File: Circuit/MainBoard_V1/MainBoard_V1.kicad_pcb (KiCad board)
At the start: 2 copper layers, 56 x 65 mm, 91 parts, among them J1 Conn_01x07, J10 Conn_01x04, J11 Conn_01x04, J12 Conn_01x04, J2 Raspberry_Pi_2_3, J3 Conn_01x04, J4 Conn_01x04, J5 Conn_01x04, J6 Conn_01x04, J7 Conn_01x04, J8 Conn_01x04, J9 Conn_01x04, Q1 Q_PMOS_GDS, Q2 Q_PMOS_GDS, Q3 BSS138, SW1 SW_Push, SW2 SW_Push, SW5 SW_Push, SW6 SW_Push, U1 LM1117MP-3.3, U11 LM78M05_TO252, U2 STM32F446RETx, U3 MPU-6050, Y1 CSTNE16M0V530000R0

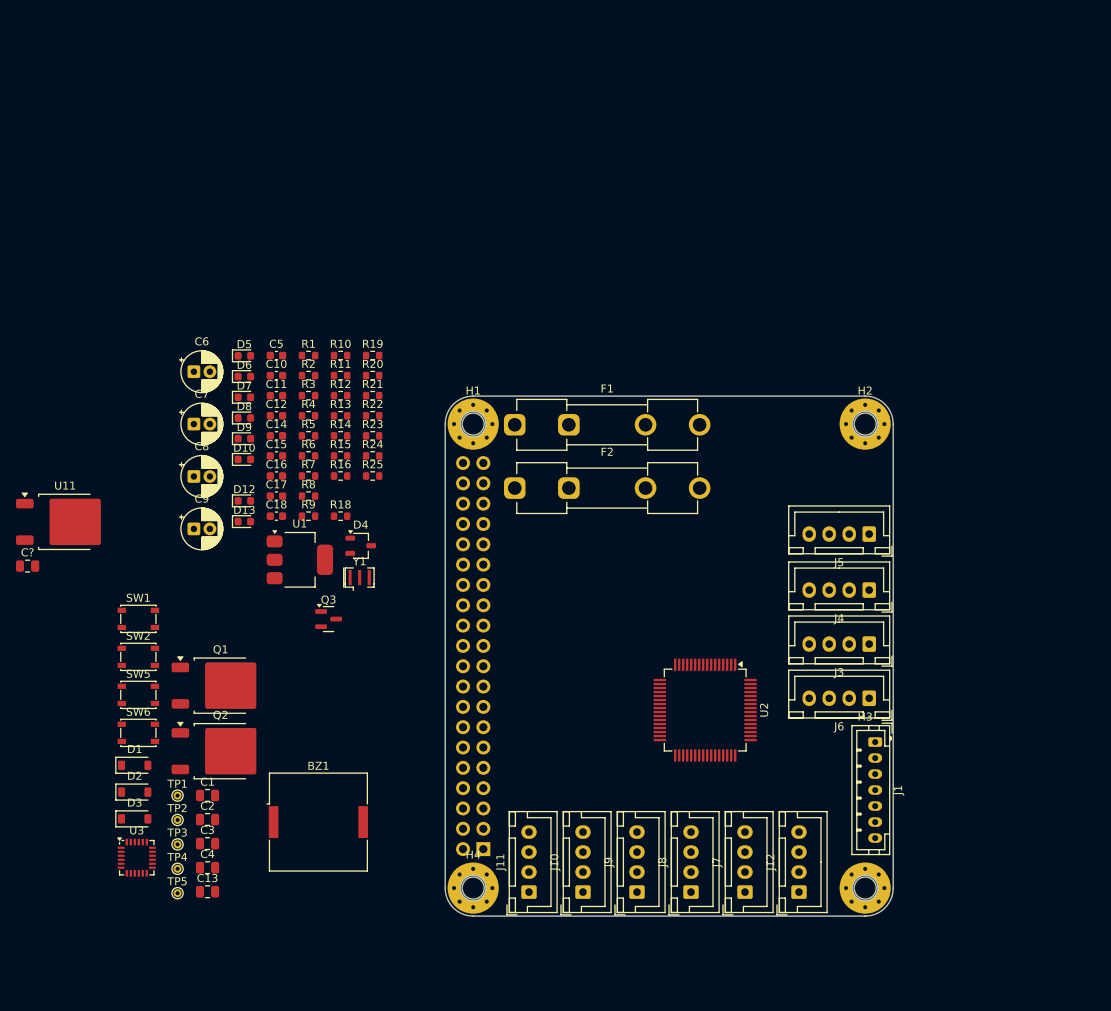
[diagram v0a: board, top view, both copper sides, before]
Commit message: 配線と配置を進めた
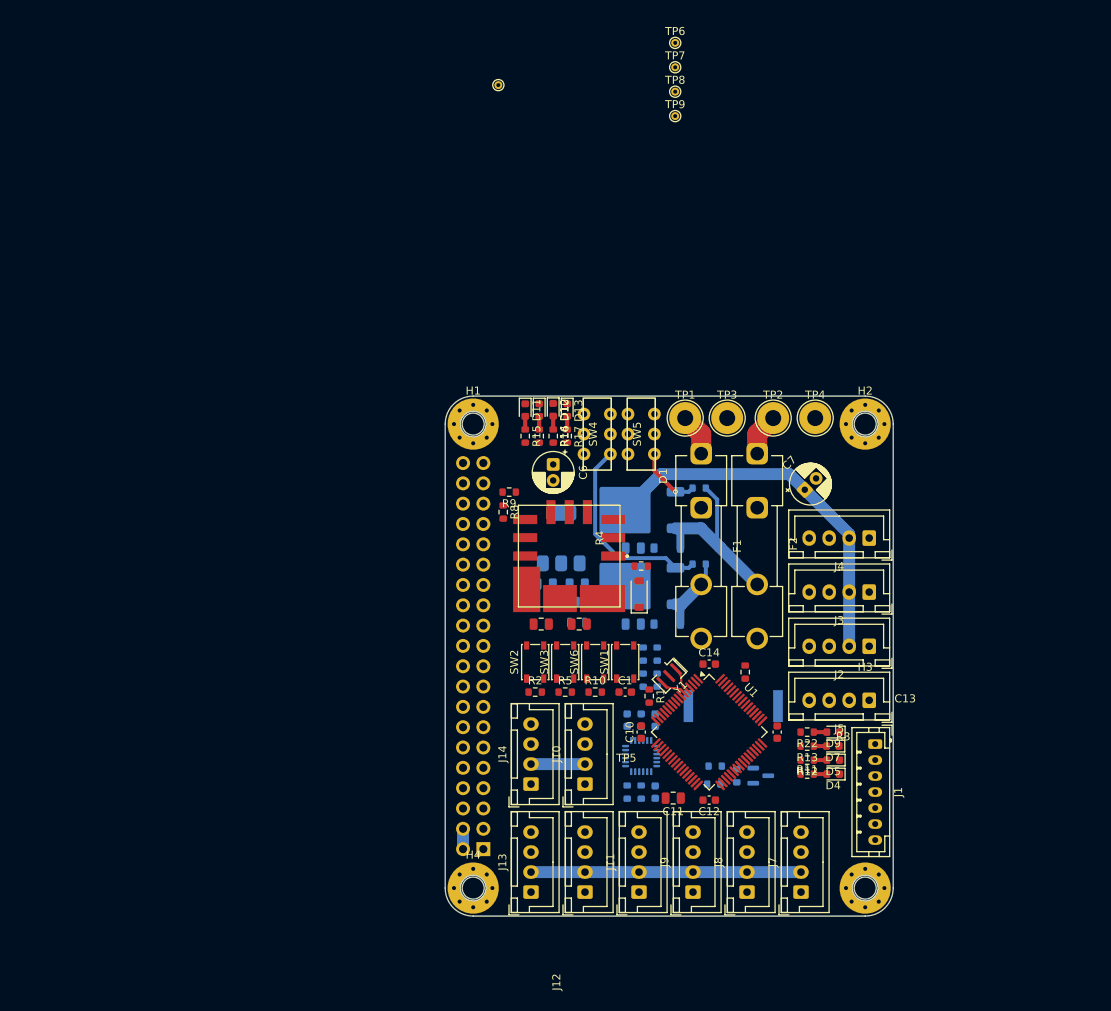
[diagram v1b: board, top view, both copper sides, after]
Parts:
- removed C?: 10u, Capacitor_SMD:C_0805_2012Metric
- removed U11: LM78M05_TO252, Package_TO_SOT_SMD:TO-252-2
- added D11: LED, LED_SMD:LED_0603_1608Metric, F.Cu at (109.5, 122.2)
- added J13: Conn_01x04, Connector_JST:JST_XH_B4B-XH-A_1x04_P2.50mm_Vertical, F.Cu at (110.2, 182.5)
- added J14: Conn_01x04, Connector_JST:JST_XH_B4B-XH-A_1x04_P2.50mm_Vertical, F.Cu at (110.2, 169.0)
- added MD1: OKL-T_6-W12N-C, 0-MyLibrary:MURATA_OKL-T-6-W12N-C_0, F.Cu at (115.0, 140.5)
- added R17: 10k, Resistor_SMD:R_0603_1608Metric, F.Cu at (114.8, 125.5)
- added R26: 4.7k, Resistor_SMD:R_0603_1608Metric, B.Cu at (122.2, 170.0)
- added R27: 4.7k, Resistor_SMD:R_0603_1608Metric, B.Cu at (124.0, 170.0)
- added SW3: SW_Push, Button_Switch_SMD:SW_SPST_PTS810, F.Cu at (114.5, 153.8)
- added SW4: SW_Slide_DPDT, 0-MyLibrary:IS-2235, F.Cu at (118.5, 125.2)
- added TP6: TestPoint, TestPoint:TestPoint_THTPad_D1.0mm_Drill0.5mm, F.Cu at (128.2, 76.3)
- added TP7: TestPoint, TestPoint:TestPoint_THTPad_D1.0mm_Drill0.5mm, F.Cu at (128.2, 79.4)
- added TP8: TestPoint, TestPoint:TestPoint_THTPad_D1.0mm_Drill0.5mm, F.Cu at (128.2, 82.5)
- added TP9: TestPoint, TestPoint:TestPoint_THTPad_D1.0mm_Drill0.5mm, F.Cu at (128.2, 85.5)
- BZ1, C15, C16, C17, C18, C4, D2, D3, Q1, Q2, Q3, R19, R21, R6, R7, U3: moved to B.Cu
- C1: value 10u -> 0.1uf; footprint Capacitor_SMD:C_0805_2012Metric -> Capacitor_SMD:C_0603_1608Metric
- C11: value 0.1uf -> 4.7u; footprint Capacitor_SMD:C_0603_1608Metric -> Capacitor_SMD:C_0805_2012Metric
- C13: value 4.7u -> 0.1uf; footprint Capacitor_SMD:C_0805_2012Metric -> Capacitor_SMD:C_0603_1608Metric
- C5: value 0.1uf -> 10u; footprint Capacitor_SMD:C_0603_1608Metric -> Capacitor_SMD:C_0805_2012Metric; moved to B.Cu
- C8, C9: value 100uf -> 10u; footprint Capacitor_THT:CP_Radial_D5.0mm_P2.00mm -> Capacitor_SMD:C_0805_2012Metric; moved to B.Cu
- D4: value CH213K -> LED; footprint Package_TO_SOT_SMD:TSOT-23 -> LED_SMD:LED_0603_1608Metric
- D6: value LED -> 1N4148W; footprint LED_SMD:LED_0603_1608Metric -> Diode_SMD:D_SOD-123; moved to B.Cu
- D8: value LED -> CH213K; footprint LED_SMD:LED_0603_1608Metric -> Package_TO_SOT_SMD:TSOT-23; moved to B.Cu
- J2: value Raspberry_Pi_2_3 -> Conn_01x04; footprint 0-MyLibrary:raspberreyPi_2_3 -> Connector_JST:JST_XH_B4B-XH-A_1x04_P2.50mm_Vertical
- J6: value Conn_01x04 -> Raspberry_Pi_2_3; footprint Connector_JST:JST_XH_B4B-XH-A_1x04_P2.50mm_Vertical -> 0-MyLibrary:raspberreyPi_2_3
- R12, R8: value 10k -> 1k
- R16: value 1k -> 10k
- R18, R20: value 1k -> 10k; moved to B.Cu
- R22: value 10 -> 1k
- R23: value 10k -> 1k; moved to B.Cu
- R24: value 4.7k -> 10; moved to B.Cu
- R25: value 4.7k -> 10k; moved to B.Cu
- R9: value 10k -> 330
- SW5: value SW_Push -> SW_Slide_DPDT; footprint Button_Switch_SMD:SW_SPST_PTS810 -> 0-MyLibrary:IS-2235
- TP1, TP2, TP3, TP4: footprint TestPoint:TestPoint_THTPad_D1.0mm_Drill0.5mm -> TestPoint:TestPoint_THTPad_D4.0mm_Drill2.0mm
- U1: value LM1117MP-3.3 -> STM32F446RETx; footprint Package_TO_SOT_SMD:SOT-223-3_TabPin2 -> Package_QFP:LQFP-64_10x10mm_P0.5mm
- U2: value STM32F446RETx -> LM1117MP-3.3; footprint Package_QFP:LQFP-64_10x10mm_P0.5mm -> Package_TO_SOT_SMD:SOT-223-3_TabPin2; moved to B.Cu
- moved TP5 108.7 mm to (106.1, 81.6)
- moved TP4 97.6 mm to (145.8, 123.2)
- moved TP2 89.8 mm to (140.5, 123.2)
- moved D5 89.3 mm to (148.0, 166.0), turned to 180 degrees
- moved TP3 86.9 mm to (134.8, 123.2)
- moved D7 85.5 mm to (148.0, 164.2), turned to 180 degrees
- moved D9 82.2 mm to (148.0, 162.5), turned to 180 degrees
- moved TP1 79.1 mm to (129.5, 123.2)
- moved C7 76.8 mm to (144.4, 132.2), turned to 45 degrees
- moved R11 76.7 mm to (144.8, 167.8), turned to 180 degrees
- moved D3 74.7 mm to (127.2, 139.5), turned to 180 degrees
- moved R12 74.0 mm to (144.8, 166.0), turned to 180 degrees
- moved C13 73.9 mm to (141.0, 162.5), turned to -90 degrees
- moved C12 72.3 mm to (132.5, 171.0), turned to 180 degrees
- moved R13 71.5 mm to (144.8, 164.2), turned to 180 degrees
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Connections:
- C1 pad 1: VCC -> GND
- C1 pad 2: GND -> NRST
- C11 pad 1: +3V3 -> Net-(U1-VCAP_1)
- C11 pad 2: GND1 -> GND
- C12 pad 1: GND1 -> GND
- C13 pad 1: Net-(U2-VCAP_1) -> GND
- C13 pad 2: GND -> +3V3
- C15 pad 1: GND -> +3V3
- C15 pad 2: +3V3 -> GND
- C2 pad 1: VCCP -> GND
- C2 pad 2: GNDP -> VCC
- C3 pad 2: +5V -> GND
- C4 pad 1: Net-(D1-A) -> VCC
- C5 pad 1: GND -> VCCP
- C5 pad 2: NRST -> GNDP
- C8 pad 1: VCC -> GND
- C8 pad 2: GND -> +5V
- C9 pad 1: VCCP -> Net-(D6-A)
- C9 pad 2: GNDP -> GND
- D1 pad 1: +5V -> VCC
- D13 pad 1: GND -> GNDP
- D4 pad 2: +3V3 -> Net-(D4-A)
- D6 pad 1: GNDP -> +5V
- D8 pad 2: Net-(D8-A) -> +3V3
- J10 pad 3: TRIG4 -> TRIG7
- J10 pad 4: ECHO4 -> ECHO7
- J11 pad 3: TRIG5 -> TRIG4
- J11 pad 4: ECHO5 -> ECHO4
- J12 pad 3: TRIG6 -> TRIG5
- J12 pad 4: ECHO6 -> ECHO5
- J2 pad 1: Net-(J2-3V3-Pad1) -> GND
- J2 pad 2: +5V -> VCCP
- J2 pad 3: unconnected-(J2-SDA/GPIO2-Pad3) -> TX2
- J2 pad 4: +5V -> RX2
- J3 pad 3: TX2 -> TX3
- J3 pad 4: RX2 -> RX3
- J4 pad 3: TX3 -> TX4
- J4 pad 4: RX3 -> RX4
- J5 pad 2: VCCP -> +3V3
- J5 pad 3: TX4 -> TX5
- J5 pad 4: RX4 -> RX5
- J6 pad 1: GND -> Net-(J6-3V3-Pad1)
- J6 pad 2: +3V3 -> +5V
- J6 pad 3: TX5 -> unconnected-(J6-SDA/GPIO2-Pad3)
- J6 pad 4: RX5 -> +5V
- R1 pad 1: Net-(D2-K) -> NRST
- R1 pad 2: Net-(Q1-G) -> +3V3
- R10 pad 1: VOLTAGE1 -> BTN3
- R10 pad 2: VCC -> GND
- R11 pad 1: GND -> Net-(D4-A)
- R11 pad 2: VOLTAGE1 -> STM_LED1
- R12 pad 1: VOLTAGE1 -> Net-(D5-A)
- R12 pad 2: VCCP -> STM_LED2
- R13 pad 1: GND2 -> Net-(D7-A)
- R13 pad 2: VOLTAGE1 -> STM_LED3
- R14 pad 1: Net-(D7-A) -> Net-(D10-A)
- R14 pad 2: STM_LED1 -> +3V3
- R15 pad 1: Net-(D9-A) -> Net-(D11-A)
- R15 pad 2: +3V3 -> +5V
- R16 pad 1: Net-(D10-A) -> Net-(D12-A)
- R16 pad 2: +5V -> VCC
- R18 pad 1: Net-(D8-A) -> VOLTAGE
- R18 pad 2: STM_LED2 -> VCC
- R19 pad 1: Net-(D12-A) -> GND
- R19 pad 2: STM_LED3 -> VOLTAGE
- R2 pad 1: Net-(D3-K) -> BTN1
- R2 pad 2: Net-(Q2-G) -> GND
- R20 pad 1: Net-(D13-A) -> VOLTAGEP
- R20 pad 2: STM_LED4 -> VCCP
- R21 pad 1: Net-(BZ1--) -> GND2
- R21 pad 2: VCC -> VOLTAGEP
- R22 pad 1: BUZZER -> Net-(D9-A)
- R22 pad 2: Net-(Q3-G) -> STM_LED4
- R23 pad 1: GND -> Net-(BZ1--)
- R23 pad 2: Net-(Q3-G) -> VCC
- R24 pad 1: +3V3 -> BUZZER
- R24 pad 2: SDA -> Net-(Q3-G)
- R25 pad 1: +3V3 -> GND
- R25 pad 2: SCL -> Net-(Q3-G)
- R3 pad 1: NRST -> GND
- R3 pad 2: +3V3 -> Net-(U1-BOOT0)
- R4 pad 1: BTN1 -> VCC
- R4 pad 2: GND -> Net-(MD1-~{ON}/OFF_CONTROL)
- R5 pad 1: GND -> BTN2
- R5 pad 2: Net-(U2-BOOT0) -> GND
- R6 pad 1: BTN2 -> Net-(D2-K)
- R6 pad 2: GND -> Net-(Q1-G)
- R7 pad 1: BTN3 -> Net-(D3-K)
- R7 pad 2: GND -> Net-(Q2-G)
- R8 pad 1: Net-(D5-A) -> Net-(R8-Pad1)
- R8 pad 2: VCC -> Net-(MD1-TRIM)
- R9 pad 1: Net-(D6-A) -> GND
- R9 pad 2: VCCP -> Net-(R8-Pad1)
- SW5 pad 1: BTN2 -> Net-(Q2-G)
- SW5 pad 2: +3V3 -> GNDP
- TP1 pad 1: SDA -> +BATT
- TP2 pad 1: SCL -> +BATTP
- TP3 pad 1: +5V -> GND
- TP4 pad 1: +3V3 -> GNDP
- TP5 pad 1: GND -> SDA
- U1 pad 1: GND -> +3V3
- U1 pad 2: Net-(D1-A) -> unconnected-(U1-PC13-Pad2)
- U1 pad 3: +5V -> unconnected-(U1-PC14-Pad3)
- U2 pad 1: +3V3 -> GND
- U2 pad 2: unconnected-(U2-PC13-Pad2) -> Net-(D6-A)
- U2 pad 3: unconnected-(U2-PC14-Pad3) -> +5V
- Y1 pad 1: Net-(U2-PH0) -> Net-(U1-PH0)
- Y1 pad 3: Net-(U2-PH1) -> Net-(U1-PH1)
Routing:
- net VCCP: track 0.00 -> 47.0 mm
- net +3V3: track 0.00 -> 40.5 mm
- net Net-(Q1-G): track 0.00 -> 24.9 mm
- net Net-(D3-K): track 0.00 -> 23.5 mm
- net Net-(D2-K): track 0.00 -> 9.75 mm
- net Net-(Q2-G): track 0.00 -> 8.14 mm, vias 0 -> 1
- net +BATTP: track 0.00 -> 5.27 mm
- net +BATT: track 0.00 -> 5.27 mm
- net Net-(U1-PH1): track 0.00 -> 3.12 mm
- net Net-(U1-PH0): track 0.00 -> 3.05 mm
- net +5V: track 0.00 -> 2.54 mm
- net Net-(D12-A): track 0.00 -> 1.67 mm
- net Net-(D9-A): track 0.00 -> 1.64 mm
- net Net-(D5-A): track 0.00 -> 1.64 mm
- net Net-(D4-A): track 0.00 -> 1.64 mm
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
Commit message: LED用のコネクタ追加
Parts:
- added J15: Conn_01x02, Connector_JST:JST_XH_B2B-XH-A_1x02_P2.50mm_Vertical, F.Cu at (117.0, 160.5)
- added J16: Conn_01x02, Connector_JST:JST_XH_B2B-XH-A_1x02_P2.50mm_Vertical, F.Cu at (110.2, 160.5)
- added Q4: BSS138, Package_TO_SOT_SMD:SOT-23, B.Cu at (114.0, 168.0)
- added Q5: BSS138, Package_TO_SOT_SMD:SOT-23, B.Cu at (107.2, 168.0)
- added Q6: BSS138, Package_TO_SOT_SMD:SOT-23, B.Cu at (114.0, 159.5)
- added Q7: BSS138, Package_TO_SOT_SMD:SOT-23, B.Cu at (107.2, 159.5)
- added R28: 10, Resistor_SMD:R_0603_1608Metric, B.Cu at (107.2, 163.5)
- added R29: 10k, Resistor_SMD:R_0603_1608Metric, B.Cu at (107.2, 165.2)
- added R30: 10, Resistor_SMD:R_0603_1608Metric, B.Cu at (114.0, 155.0)
- added R31: 10k, Resistor_SMD:R_0603_1608Metric, B.Cu at (114.0, 156.8)
- added R32: 4.7k, Resistor_SMD:R_0603_1608Metric, B.Cu at (123.2, 170.0)
- added R33: 4.7k, Resistor_SMD:R_0603_1608Metric, B.Cu at (125.0, 170.0)
- added R34: 10, Resistor_SMD:R_0603_1608Metric, B.Cu at (107.2, 155.0)
- added R35: 10k, Resistor_SMD:R_0603_1608Metric, B.Cu at (107.2, 156.8)
- J13, J14: value Conn_01x04 -> Conn_01x02; footprint Connector_JST:JST_XH_B4B-XH-A_1x04_P2.50mm_Vertical -> Connector_JST:JST_XH_B2B-XH-A_1x02_P2.50mm_Vertical
- R26: value 4.7k -> 10
- R27: value 4.7k -> 10k
- moved TP5 23.5 mm to (128.2, 73.8)
- moved C6 21.0 mm to (108.2, 149.5)
- moved J10 15.1 mm to (123.7, 182.5)
- moved J13 15.1 mm to (117.0, 169.0)
- moved R27 11.1 mm to (114.0, 165.2), turned to 180 degrees
- moved R26 10.5 mm to (114.0, 163.5), turned to 180 degrees
- moved J11 6.75 mm to (117.0, 182.5)
- moved J12 6.75 mm to (110.2, 182.5)
- moved C1 3.95 mm to (124.2, 154.2)
- moved R10 3.95 mm to (120.5, 154.2)
- moved R2 3.95 mm to (113.0, 154.2)
- moved R5 3.95 mm to (116.8, 154.2)
- moved SW1 3.95 mm to (124.2, 150.5)
- moved SW2 3.95 mm to (113.0, 150.5)
- moved SW3 3.95 mm to (116.8, 150.5)
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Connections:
- J10 pad 3: TRIG7 -> TRIG4
- J10 pad 4: ECHO7 -> ECHO4
- J11 pad 3: TRIG4 -> TRIG5
- J11 pad 4: ECHO4 -> ECHO5
- J12 pad 3: TRIG5 -> TRIG6
- J12 pad 4: ECHO5 -> ECHO6
- J13 pad 1: GND -> LED1
- J13 pad 2: +3V3 -> +5V
- J14 pad 1: GND -> LED2
- J14 pad 2: +3V3 -> +5V
- R26 pad 1: +3V3 -> LED1_SIG
- R26 pad 2: SDA -> Net-(Q4-G)
- R27 pad 1: +3V3 -> GND
- R27 pad 2: SCL -> Net-(Q4-G)
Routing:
- net +3V3: track 40.5 -> 0.00 mm

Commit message: 配線進捗
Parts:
- moved R10 58.5 mm to (179.0, 154.0)
- moved R5 58.5 mm to (175.2, 154.0)
- moved SW3 58.5 mm to (175.2, 150.2)
- moved SW6 58.5 mm to (179.0, 150.2)
- moved C1 30.9 mm to (109.2, 127.2)
- moved SW1 30.9 mm to (109.2, 123.5)
- moved R2 27.0 mm to (113.2, 127.2)
- moved SW2 27.0 mm to (113.2, 123.5)
- moved C6 17.9 mm to (90.5, 147.3)
- moved C13 14.8 mm to (127.0, 157.8), turned to -135 degrees
- moved J4 13.5 mm to (152.5, 151.8)
- moved J2 13.5 mm to (152.5, 138.3)
- moved D10 9.30 mm to (112.2, 131.5)
- moved D11 9.30 mm to (110.5, 131.5)
- moved D12 9.30 mm to (114.0, 131.5)
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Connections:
- J10 pad 3: TRIG4 -> ECHO4
- J10 pad 4: ECHO4 -> TRIG4
- J11 pad 3: TRIG5 -> ECHO5
- J11 pad 4: ECHO5 -> TRIG5
- J12 pad 3: TRIG6 -> ECHO6
- J12 pad 4: ECHO6 -> TRIG6
- J3 pad 3: TX3 -> TX4
- J3 pad 4: RX3 -> RX4
- J4 pad 3: TX4 -> TX5
- J4 pad 4: RX4 -> RX5
- J5 pad 3: TX5 -> TX3
- J5 pad 4: RX5 -> RX3
- J7 pad 3: TRIG1 -> ECHO1
- J7 pad 4: ECHO1 -> TRIG1
- J8 pad 3: TRIG2 -> ECHO2
- J8 pad 4: ECHO2 -> TRIG2
- J9 pad 3: TRIG3 -> ECHO3
- J9 pad 4: ECHO3 -> TRIG3
- U1 pad 22: unconnected-(U1-PA6-Pad22) -> LED4_SIG
- U1 pad 23: unconnected-(U1-PA7-Pad23) -> LED3_SIG
- U1 pad 26: unconnected-(U1-PB0-Pad26) -> LED2_SIG
- U1 pad 27: unconnected-(U1-PB1-Pad27) -> LED1_SIG
- U1 pad 28: unconnected-(U1-PB2-Pad28) -> TRIG6
- U1 pad 29: unconnected-(U1-PB10-Pad29) -> ECHO6
- U1 pad 33: unconnected-(U1-PB12-Pad33) -> TRIG5
- U1 pad 34: unconnected-(U1-PB13-Pad34) -> ECHO5
- U1 pad 35: unconnected-(U1-PB14-Pad35) -> TRIG4
- U1 pad 36: unconnected-(U1-PB15-Pad36) -> ECHO4
- U1 pad 37: TX6 -> RAS_RX
- U1 pad 38: RX6 -> RAS_TX  
- U1 pad 39: unconnected-(U1-PC8-Pad39) -> TRIG3
- U1 pad 40: unconnected-(U1-PC9-Pad40) -> ECHO3
- U1 pad 41: unconnected-(U1-PA8-Pad41) -> ECHO2
- U1 pad 42: TX1 -> PC_RX
- U1 pad 43: RX1 -> PC_TX
- U1 pad 44: unconnected-(U1-PA11-Pad44) -> TRIG2
- U1 pad 45: unconnected-(U1-PA12-Pad45) -> ECHO1
- U1 pad 50: unconnected-(U1-PA15-Pad50) -> TRIG1
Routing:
- net RAS_TX  : track 0.00 -> 34.2 mm, vias 0 -> 1
- net RAS_RX: track 0.00 -> 33.7 mm, vias 0 -> 1
- net RX2: track 0.00 -> 32.1 mm
- net TX2: track 0.00 -> 31.0 mm
- net TX4: track 0.00 -> 25.0 mm
- net RX4: track 0.00 -> 24.2 mm
- net SWDIO: track 0.00 -> 24.0 mm
- net PC_RX: track 0.00 -> 23.6 mm, vias 0 -> 1
- net PC_TX: track 0.00 -> 22.0 mm, vias 0 -> 1
- net ECHO6: track 0.00 -> 21.9 mm
- net VCC: track 0.00 -> 21.8 mm
- net TRIG6: track 0.00 -> 21.0 mm
- net +5V: track 2.54 -> 21.8 mm
- net TX5: track 0.00 -> 18.2 mm
- net ECHO5: track 0.00 -> 16.7 mm
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
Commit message: 進捗
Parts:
- removed R10: 10k, Resistor_SMD:R_0603_1608Metric
- removed SW6: SW_Push, Button_Switch_SMD:SW_SPST_PTS810
- added J17: Conn_01x04, Connector_JST:JST_XH_B4B-XH-A_1x04_P2.50mm_Vertical, F.Cu at (117.0, 182.5)
- added J18: Conn_01x02, Connector_JST:JST_XH_B2B-XH-A_1x02_P2.50mm_Vertical, F.Cu at (110.2, 182.5)
- added J19: Conn_01x02, Connector_JST:JST_XH_B2B-XH-A_1x02_P2.50mm_Vertical, F.Cu at (110.2, 174.0)
- added J20: Conn_01x02, Connector_JST:JST_XH_B2B-XH-A_1x02_P2.50mm_Vertical, F.Cu at (110.2, 165.5)
- added J21: Conn_01x02, Connector_JST:JST_XH_B2B-XH-A_1x02_P2.50mm_Vertical, F.Cu at (110.2, 157.0)
- C11: moved to B.Cu
- J1: value Conn_01x07 -> Conn_01x02; footprint Connector_JST:JST_PH_B7B-PH-K_1x07_P2.00mm_Vertical -> Connector_JST:JST_PH_B2B-PH-K_1x02_P2.00mm_Vertical
- J10, J11, J12: value Conn_01x04 -> Conn_01x03; footprint Connector_JST:JST_XH_B4B-XH-A_1x04_P2.50mm_Vertical -> Connector_JST:JST_XH_B3B-XH-A_1x03_P2.50mm_Vertical
- J13, J14, J15, J16: value Conn_01x02 -> Conn_01x04; footprint Connector_JST:JST_XH_B2B-XH-A_1x02_P2.50mm_Vertical -> Connector_JST:JST_XH_B4B-XH-A_1x04_P2.50mm_Vertical
- J2, J3: value Conn_01x04 -> Conn_01x02; footprint Connector_JST:JST_XH_B4B-XH-A_1x04_P2.50mm_Vertical -> Connector_JST:JST_PH_B2B-PH-K_1x02_P2.00mm_Vertical
- J5, J7: value Conn_01x04 -> Conn_01x02; footprint Connector_JST:JST_XH_B4B-XH-A_1x04_P2.50mm_Vertical -> Connector_JST:JST_XH_B2B-XH-A_1x02_P2.50mm_Vertical
- J6: value Raspberry_Pi_2_3 -> Conn_01x02; footprint 0-MyLibrary:raspberreyPi_2_3 -> Connector_JST:JST_XH_B2B-XH-A_1x02_P2.50mm_Vertical
- J8: value Conn_01x04 -> Conn_01x07; footprint Connector_JST:JST_XH_B4B-XH-A_1x04_P2.50mm_Vertical -> Connector_JST:JST_PH_B7B-PH-K_1x07_P2.00mm_Vertical
- J9: value Conn_01x04 -> Raspberry_Pi_2_3; footprint Connector_JST:JST_XH_B4B-XH-A_1x04_P2.50mm_Vertical -> 0-MyLibrary:raspberreyPi_2_3
- moved J6 54.0 mm to (152.5, 131.5), turned to 180 degrees
- moved SW1 51.3 mm to (152.5, 151.0), turned to 0 degrees
- moved SW2 50.3 mm to (152.5, 155.0), turned to 180 degrees
- moved C1 46.1 mm to (148.8, 151.0), turned to -90 degrees
- moved R2 45.1 mm to (148.8, 155.0), turned to 90 degrees
- moved J7 44.8 mm to (152.5, 138.5), turned to 180 degrees
- moved J9 40.3 mm to (103.0, 153.0)
- moved C7 36.5 mm to (108.0, 129.8), turned to 0 degrees
- moved J1 33.4 mm to (143.7, 132.0), turned to 90 degrees
- moved C6 30.7 mm to (115.0, 128.8)
- moved J13 30.2 mm to (144.0, 182.5)
- moved J14 30.2 mm to (137.2, 182.5)
- moved J12 28.9 mm to (117.2, 154.5), turned to 0 degrees
- moved R5 27.0 mm to (148.8, 159.0), turned to 90 degrees
- moved J15 25.8 mm to (130.5, 182.5)
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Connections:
- J1 pad 1: GND -> TX2
- J1 pad 2: +3V3 -> RX2
- J10 pad 3: ECHO4 -> ADC1
- J11 pad 3: ECHO5 -> ADC2
- J12 pad 3: ECHO6 -> ADC3
- J13 pad 1: LED1 -> GND
- J13 pad 2: +5V -> +3V3
- J14 pad 1: LED2 -> GND
- J14 pad 2: +5V -> +3V3
- J15 pad 1: LED3 -> GND
- J15 pad 2: +5V -> +3V3
- J16 pad 1: LED4 -> GND
- J16 pad 2: +5V -> +3V3
- J2 pad 1: GND -> TX4
- J2 pad 2: VCCP -> RX4
- J3 pad 1: GND -> TX5
- J3 pad 2: VCCP -> RX5
- J4 pad 2: VCCP -> +5V
- J4 pad 3: TX5 -> TX3
- J4 pad 4: RX5 -> RX3
- J5 pad 1: GND -> GNDP
- J5 pad 2: +3V3 -> VCCP
- J6 pad 1: Net-(J6-3V3-Pad1) -> GNDP
- J6 pad 2: +5V -> VCCP
- J7 pad 1: GND -> GNDP
- J7 pad 2: +3V3 -> VCCP
- J8 pad 3: ECHO2 -> SWDIO
- J8 pad 4: TRIG2 -> SWCLK
- J9 pad 1: GND -> Net-(J9-3V3-Pad1)
- J9 pad 2: +3V3 -> +5V
- J9 pad 3: ECHO3 -> unconnected-(J9-SDA/GPIO2-Pad3)
- J9 pad 4: TRIG3 -> +5V
- U1 pad 2: unconnected-(U1-PC13-Pad2) -> BTN2
- U1 pad 20: unconnected-(U1-PA4-Pad20) -> ADC3
- U1 pad 21: unconnected-(U1-PA5-Pad21) -> ADC2
- U1 pad 24: unconnected-(U1-PC4-Pad24) -> ADC1
- U1 pad 28: TRIG6 -> unconnected-(U1-PB2-Pad28)
- U1 pad 29: ECHO6 -> unconnected-(U1-PB10-Pad29)
- U1 pad 3: unconnected-(U1-PC14-Pad3) -> BTN1
- U1 pad 56: unconnected-(U1-PB4-Pad56) -> STM_LED1
- U1 pad 57: unconnected-(U1-PB5-Pad57) -> STM_LED2
- U1 pad 58: unconnected-(U1-PB6-Pad58) -> STM_LED3
- U1 pad 59: unconnected-(U1-PB7-Pad59) -> STM_LED4
- U1 pad 61: unconnected-(U1-PB8-Pad61) -> SCL
- U1 pad 62: unconnected-(U1-PB9-Pad62) -> SDA
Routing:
- net +3V3: track 15.0 -> 80.1 mm, vias 0 -> 4
- net NRST: track 3.69 -> 51.0 mm, vias 0 -> 4
- net +5V: track 21.8 -> 53.8 mm
- net BTN2: track 0.00 -> 26.5 mm, vias 0 -> 3
- net BTN1: track 0.00 -> 25.8 mm, vias 0 -> 3
- net LED1_SIG: track 0.00 -> 22.0 mm, vias 0 -> 1
- net ECHO6: track 21.9 -> 0.00 mm
- net TRIG6: track 21.0 -> 0.00 mm
- net LED4_SIG: track 0.00 -> 20.7 mm, vias 0 -> 1
- net LED2_SIG: track 0.00 -> 15.3 mm, vias 0 -> 1
- net LED3_SIG: track 0.00 -> 14.5 mm, vias 0 -> 1
- net STM_LED4: track 0.00 -> 13.0 mm, vias 0 -> 2
- net STM_LED3: track 0.00 -> 12.2 mm, vias 0 -> 2
- net STM_LED2: track 0.00 -> 11.5 mm, vias 0 -> 2
- net STM_LED1: track 0.00 -> 10.3 mm, vias 0 -> 2
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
